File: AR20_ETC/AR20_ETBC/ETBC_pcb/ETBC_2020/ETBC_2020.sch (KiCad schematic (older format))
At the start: 31 parts, among them IC1 MC33931EK, J1 Conn_02x09_Top_Bottom, Q1 NDS356AP, U1 ACM_2020

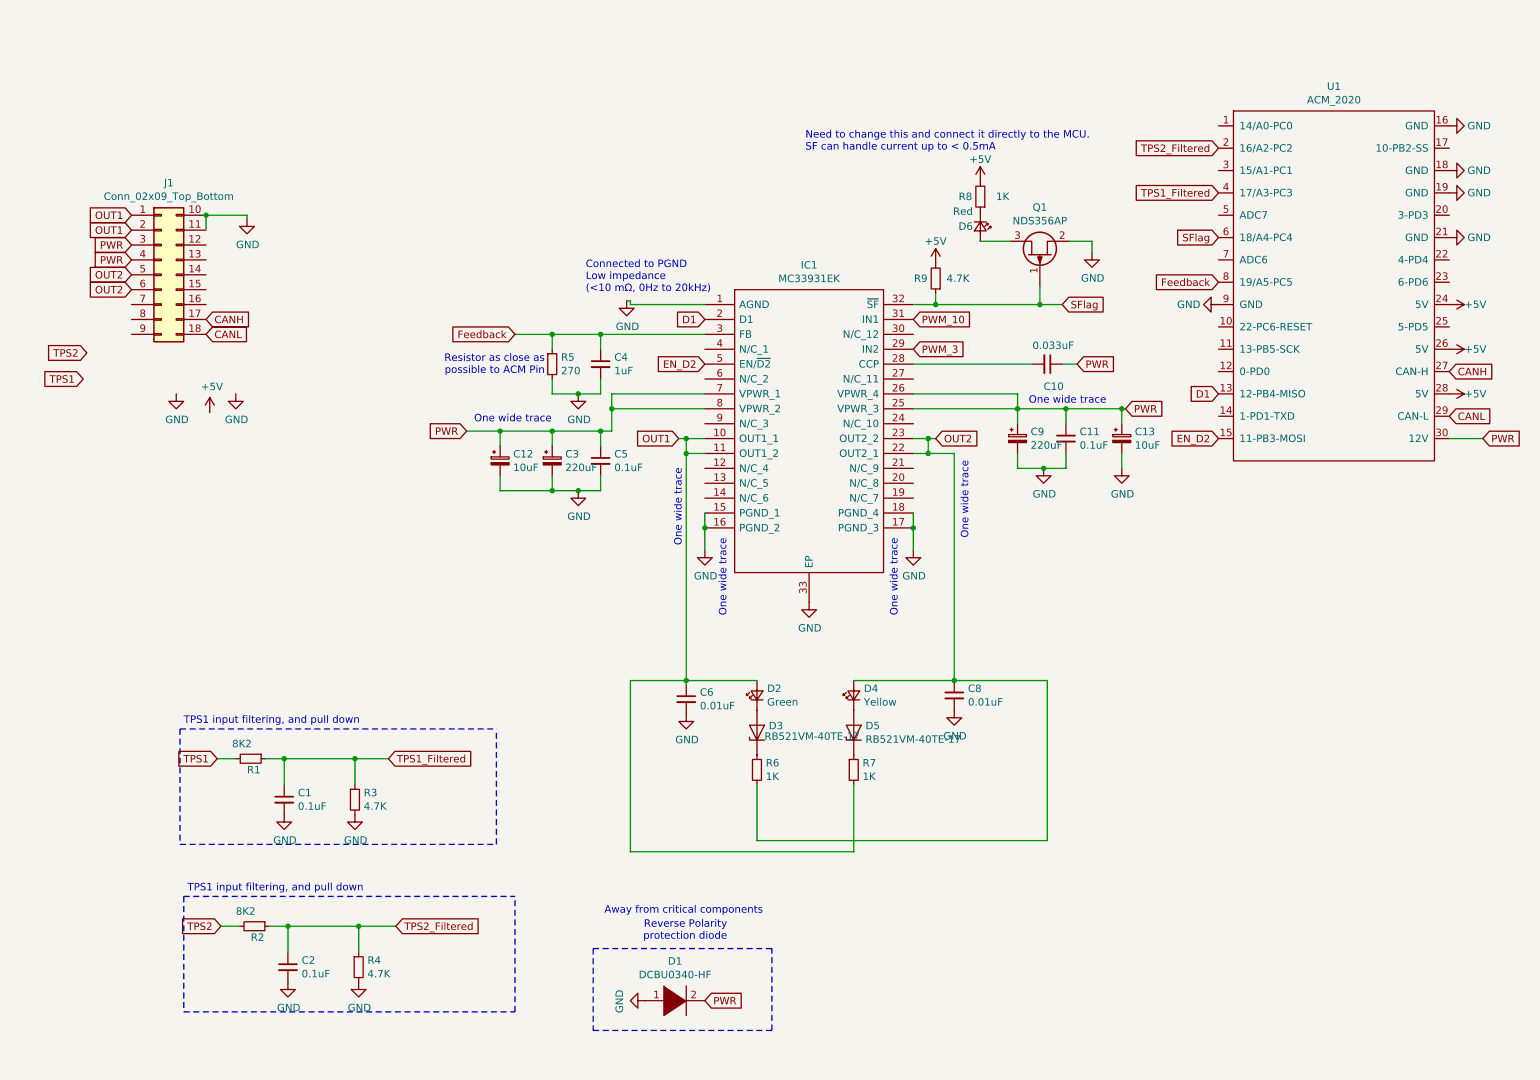
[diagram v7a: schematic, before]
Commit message: ETBC Semi complete - Evryting connected. Check description
Neec to check all footprints.
Need to check all symbols (Pin numbering correspond to footprint and datasheet)
Need to check JLCPCB DRC settings.
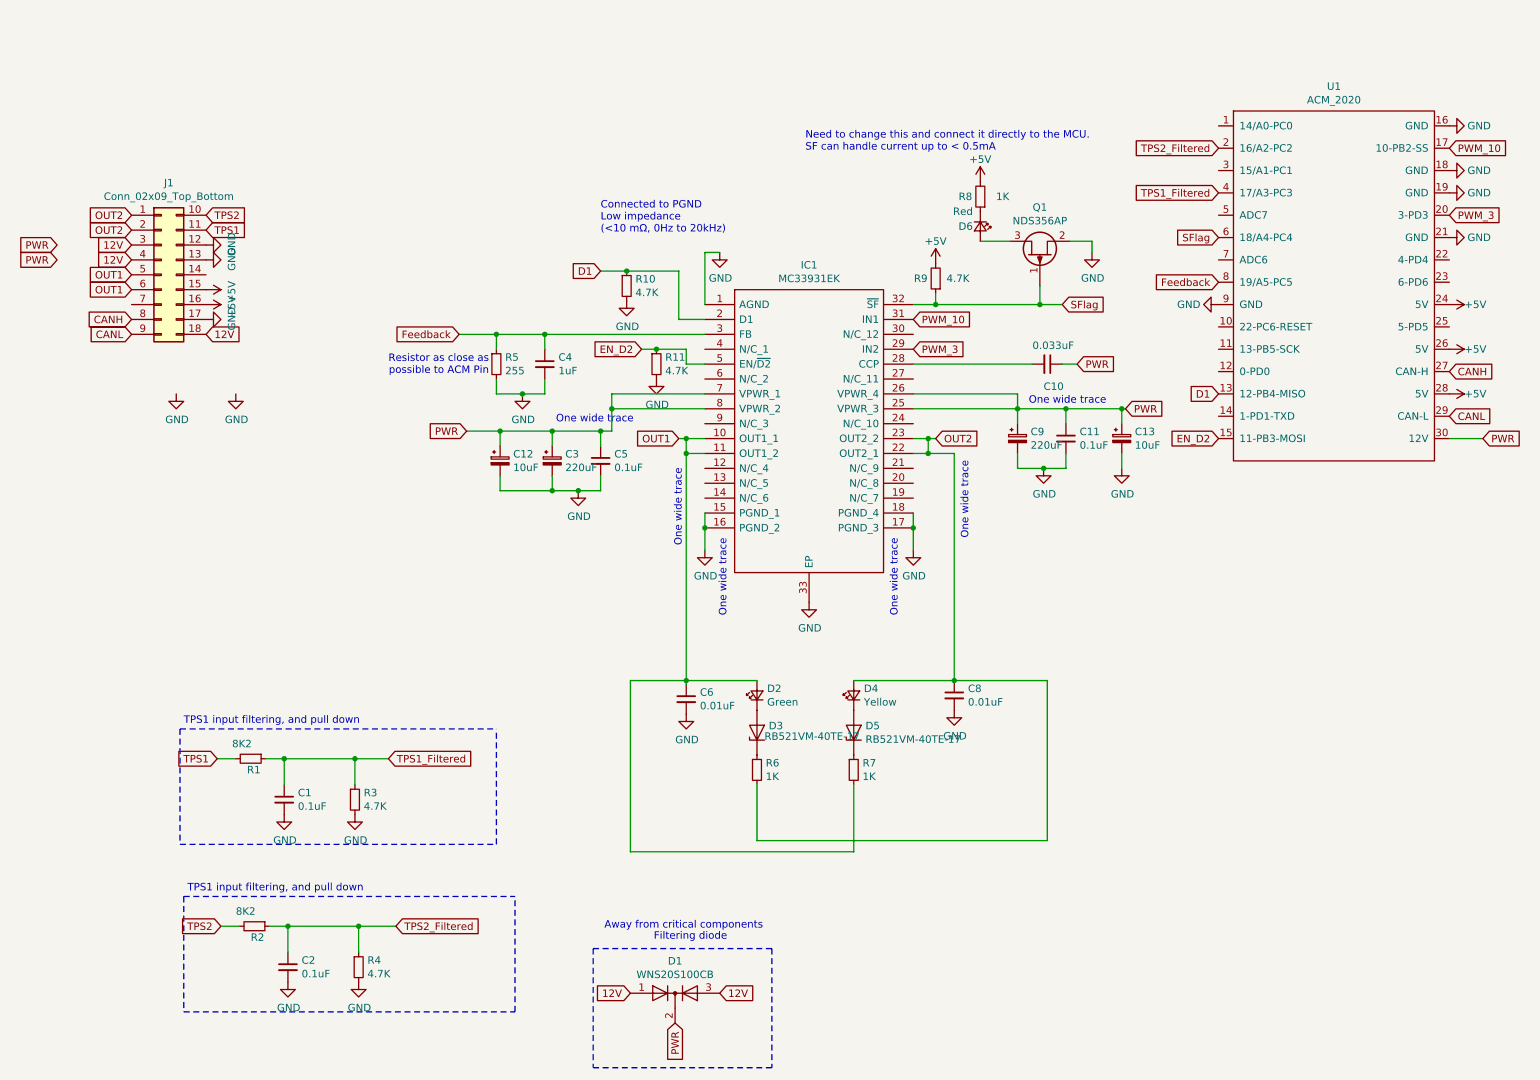
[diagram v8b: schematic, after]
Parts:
- removed D1: DCBU0340-HF, Diode_SMD:D_1206_3216Metric_Pad1.42x1.75mm_HandSolder, symbol pspice:DIODE
- added D1: WNS20S100CB, Package_TO_SOT_SMD:TO-263-3_TabPin2, symbol Device:D_x2_KCom_AKA
- added R10, R11: 4.7K, Resistor_SMD:R_0603_1608Metric_Pad1.05x0.95mm_HandSolder, symbol Device:R_Small
- D3, D5: Description Zener diode for LED -> Schottky diode for LED
- R5: value 270 -> 255
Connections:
- net +5V: now also J1.15 (Pin_15), J1.16 (Pin_16)
- net CANH: now also J1.8 (Pin_8); no longer J1.17 (Pin_17)
- net CANL: now also J1.9 (Pin_9); no longer J1.18 (Pin_18)
- net D1: now also R10.1
- net EN_D2: now also R11.1
- net GND: now also J1.12 (Pin_12), J1.13 (Pin_13), J1.17 (Pin_17), R10.2, R11.2; no longer J1.10 (Pin_10), J1.11 (Pin_11)
- net OUT1: now also J1.5 (Pin_5), J1.6 (Pin_6); no longer J1.1 (Pin_1), J1.2 (Pin_2)
- net OUT2: now also J1.1 (Pin_1), J1.2 (Pin_2); no longer J1.5 (Pin_5), J1.6 (Pin_6)
- net PWM_10: now also U1.17 (10-PB2-SS)
- net PWM_3: now also U1.20 (3-PD3)
- net PWR: now also D1.2 (K); no longer J1.3 (Pin_3), J1.4 (Pin_4)
- net TPS1: now also J1.11 (Pin_11)
- net TPS2: now also J1.10 (Pin_10)
- new net 12V: D1.1 (A), D1.3 (A), J1.18 (Pin_18), J1.3 (Pin_3), J1.4 (Pin_4)
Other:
- note added: "Filtering diode"
- note removed: "Reverse Polarity\nprotection diode"
- moved on the sheet: C4, R5
